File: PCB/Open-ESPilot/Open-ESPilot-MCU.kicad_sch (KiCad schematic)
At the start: 4 parts, among them J1 USB_C_Receptacle_USB2.0_16P, U1 ESP32-S3-WROOM-1-N8

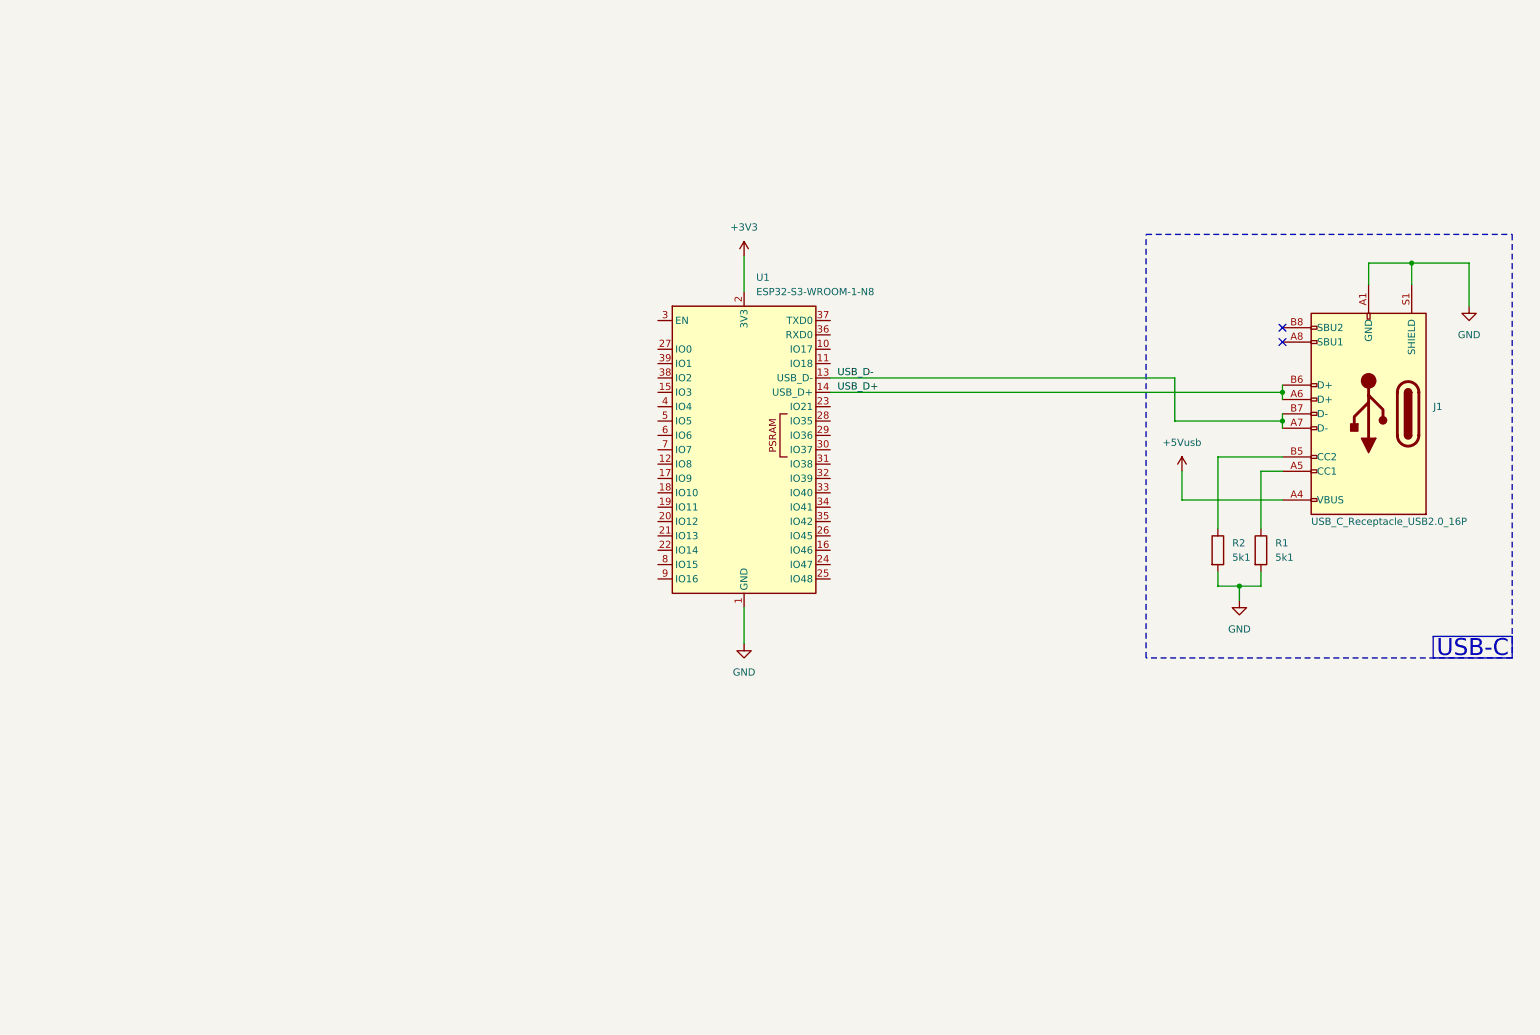
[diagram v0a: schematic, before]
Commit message: Finished schematic for the ESP32S3.
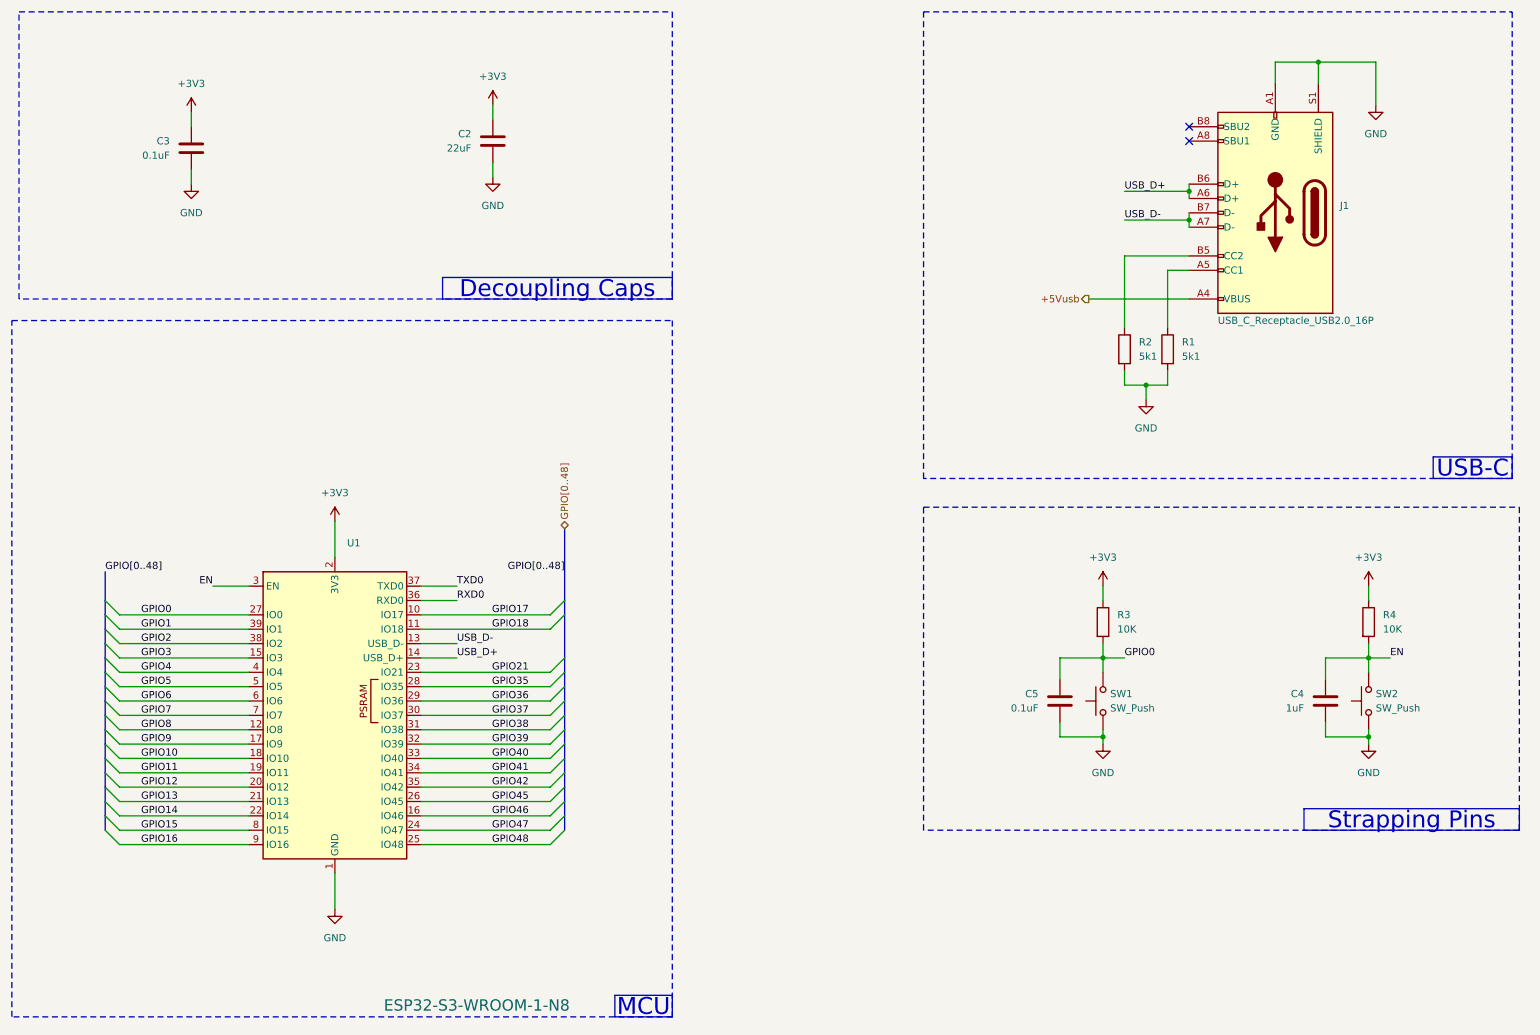
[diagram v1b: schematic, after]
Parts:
- added C2: 22uF, symbol Device:C
- added C3, C5: 0.1uF, symbol Device:C
- added C4: 1uF, symbol Device:C
- added R3, R4: 10K, symbol Device:R
- added SW1, SW2: SW_Push, symbol Switch:SW_Push
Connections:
- net +3V3: now also C2.1, C3.1, R3.1, R4.1
- net GND: now also C2.2, C3.2, C4.2, C5.2, SW1.1, SW2.1
- net GPIO17: now reaches U1.10 (IO17)
- net GPIO18: now reaches U1.11 (IO18)
- net GPIO8: now reaches U1.12 (IO8)
- net GPIO3: now reaches U1.15 (IO3)
- net GPIO46: now reaches U1.16 (IO46)
- net GPIO9: now reaches U1.17 (IO9)
- net GPIO10: now reaches U1.18 (IO10)
- net GPIO11: now reaches U1.19 (IO11)
- net GPIO12: now reaches U1.20 (IO12)
- net GPIO13: now reaches U1.21 (IO13)
- net GPIO14: now reaches U1.22 (IO14)
- net GPIO21: now reaches U1.23 (IO21)
- net GPIO47: now reaches U1.24 (IO47)
- net GPIO48: now reaches U1.25 (IO48)
- net GPIO45: now reaches U1.26 (IO45)
- net GPIO0: now reaches U1.27 (IO0)
- net GPIO0: now also C5.1, R3.2, SW1.2
- net GPIO35: now reaches U1.28 (IO35)
- net GPIO36: now reaches U1.29 (IO36)
- net EN: now reaches U1.3 (EN)
- net EN: now also C4.1, R4.2, SW2.2
- net GPIO37: now reaches U1.30 (IO37)
- net GPIO38: now reaches U1.31 (IO38)
- net GPIO39: now reaches U1.32 (IO39)
- net GPIO40: now reaches U1.33 (IO40)
- net GPIO41: now reaches U1.34 (IO41)
- net GPIO42: now reaches U1.35 (IO42)
- net RXD0: now reaches U1.36 (RXD0)
- net TXD0: now reaches U1.37 (TXD0)
- net GPIO2: now reaches U1.38 (IO2)
- net GPIO1: now reaches U1.39 (IO1)
- net GPIO4: now reaches U1.4 (IO4)
- net GPIO5: now reaches U1.5 (IO5)
- net GPIO6: now reaches U1.6 (IO6)
- net GPIO7: now reaches U1.7 (IO7)
- net GPIO15: now reaches U1.8 (IO15)
- net GPIO16: now reaches U1.9 (IO16)
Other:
- moved on the sheet: J1, R1, R2, U1

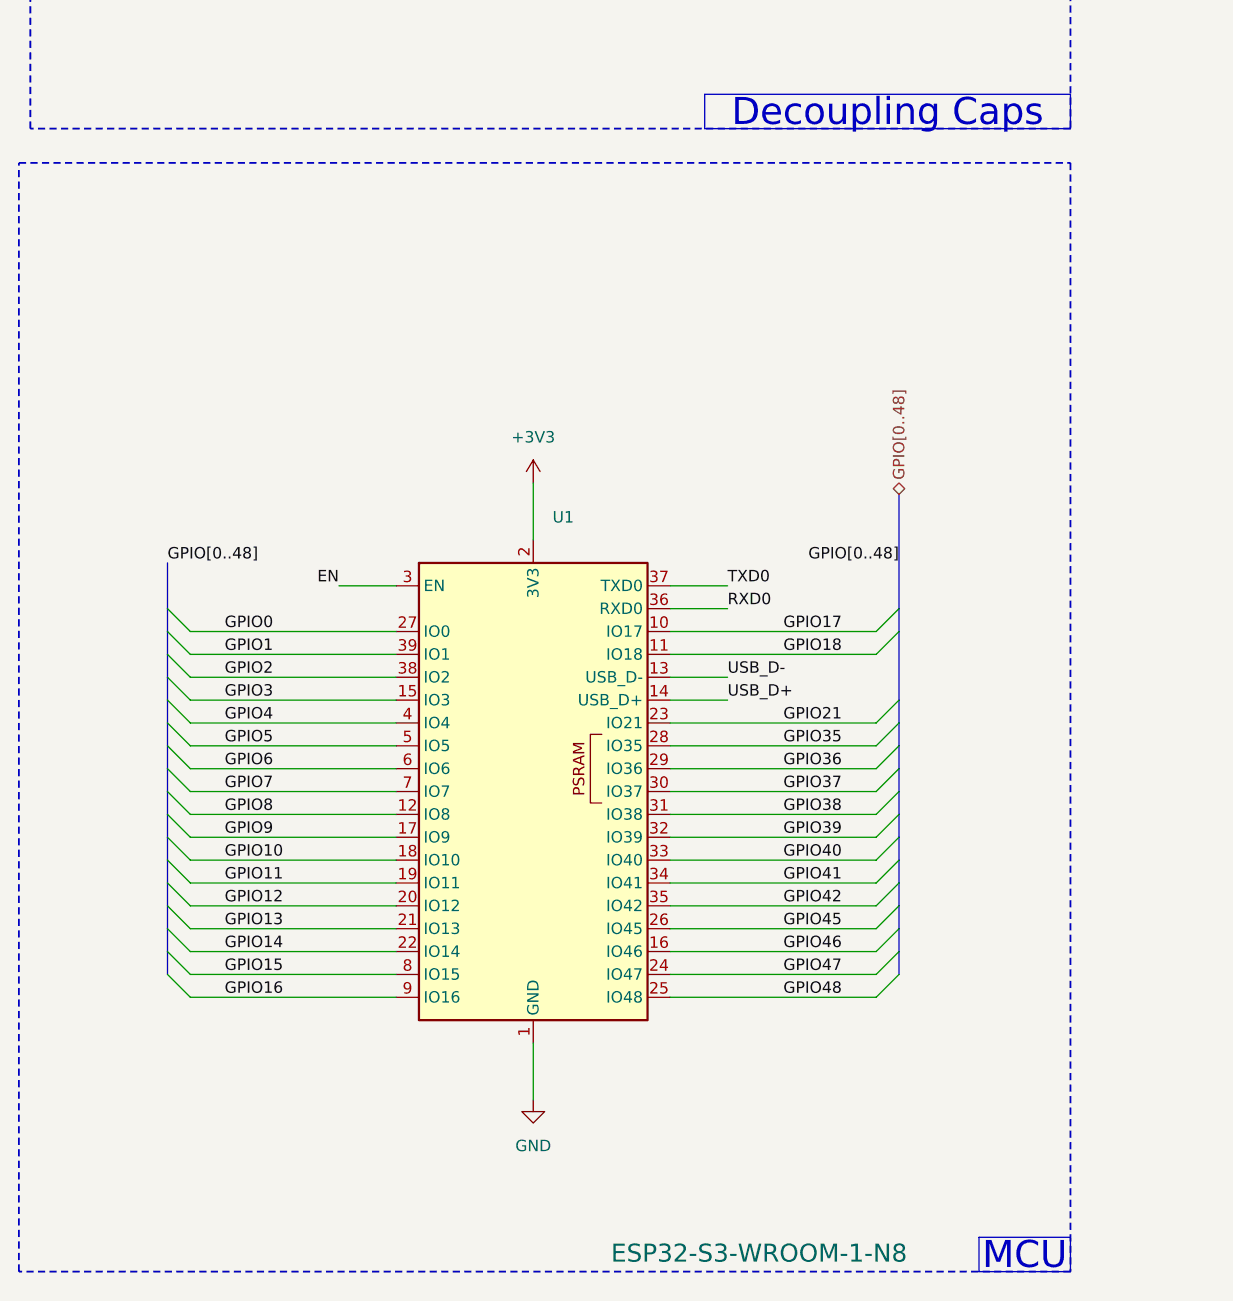
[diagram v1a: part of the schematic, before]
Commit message: Edited Pin definitions to Open ESPilot. And added the pheripherials to the schematic. Also new journal entry.
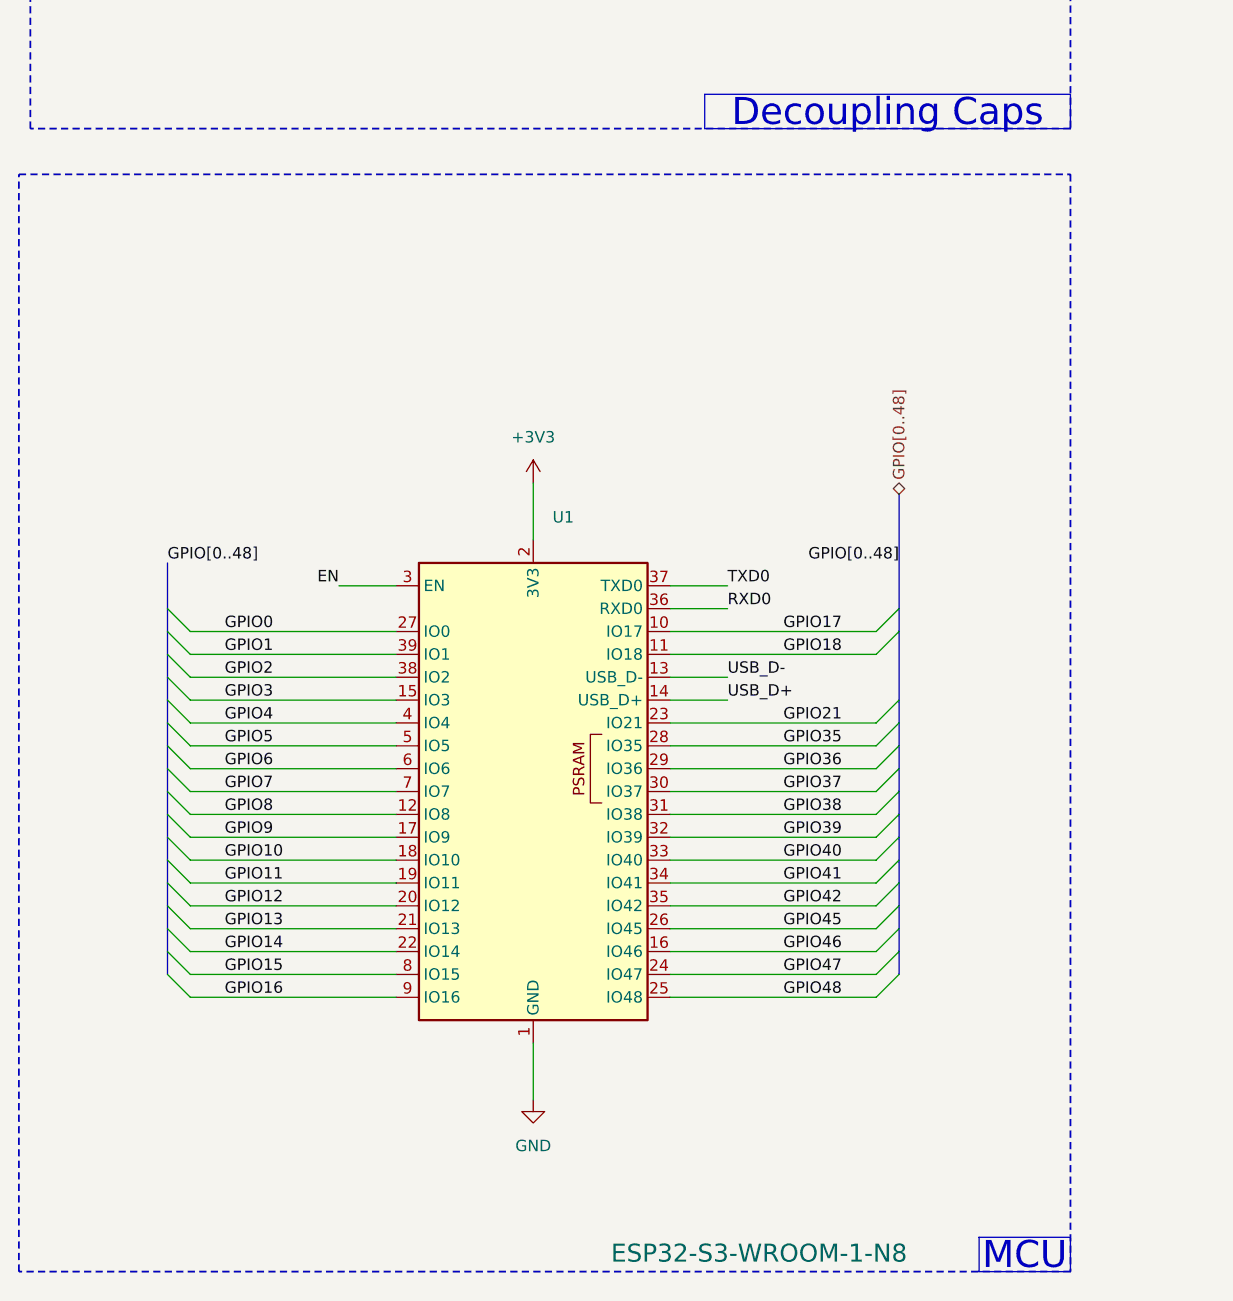
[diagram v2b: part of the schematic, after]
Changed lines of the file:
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@@
 	)
 	(rectangle
-		(start 15.24 71.12)
+		(start 15.24 72.39)
 		(end 132.08 194.31)
 		(stroke

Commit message: Schematic Fixes
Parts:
- added TP1: GPIO3, symbol Connector:TestPoint
- added TP2: GPIO45, symbol Connector:TestPoint
- added TP3: GPIO46, symbol Connector:TestPoint
- J1: footprint footprints:USB_C_Receptacle_HRO_TYPE-C-31-M-12 -> USB-C:USB_C_Receptacle_HRO_TYPE-C-31-M-12
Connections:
- net GPIO3: now also TP1.1
- net GPIO45: now also TP2.1
- net GPIO46: now also TP3.1
- net RXD0 renamed GPIO44
- net TXD0 renamed GPIO43
